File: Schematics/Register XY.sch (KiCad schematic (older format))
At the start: 0 parts

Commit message: Added XY register pair.
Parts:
- added C? (x4): 100nF, symbol Device:C
- added D? (x16): LED, symbol Device:LED
- added R? (x16): 220Ω, symbol Device:R
- added U? (x2): 74LS245, symbol 74xx:74LS245
- added U? (x2): 74F377, symbol 74xx:74LS377
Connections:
- new net: D?.1 (K), R?.1 (x16)
- new net AddressBus00: D?.2 (A), U?.19 (Q7), U?.9 (A7)
- new net AddressBus01: D?.2 (A), U?.16 (Q6), U?.8 (A6)
- new net AddressBus02: D?.2 (A), U?.15 (Q5), U?.7 (A5)
- new net AddressBus03: D?.2 (A), U?.12 (Q4), U?.6 (A4)
- new net AddressBus04: D?.2 (A), U?.5 (A3), U?.9 (Q3)
- new net AddressBus05: D?.2 (A), U?.4 (A2), U?.6 (Q2)
- new net AddressBus06: D?.2 (A), U?.3 (A1), U?.5 (Q1)
- new net AddressBus07: D?.2 (A), U?.2 (A0), U?.2 (Q0)
- new net AddressBus08: D?.2 (A), U?.19 (Q7), U?.9 (A7)
- new net AddressBus09: D?.2 (A), U?.16 (Q6), U?.8 (A6)
- new net AddressBus10: D?.2 (A), U?.15 (Q5), U?.7 (A5)
- new net AddressBus11: D?.2 (A), U?.12 (Q4), U?.6 (A4)
- new net AddressBus12: D?.2 (A), U?.5 (A3), U?.9 (Q3)
- new net AddressBus13: D?.2 (A), U?.4 (A2), U?.6 (Q2)
- new net AddressBus14: D?.2 (A), U?.3 (A1), U?.5 (Q1)
- new net AddressBus15: D?.2 (A), U?.2 (A0), U?.2 (Q0)
- new net DataBus00: U?.18 (B0), U?.18 (B0), U?.3 (D0), U?.3 (D0)
- new net DataBus01: U?.17 (B1), U?.17 (B1), U?.4 (D1), U?.4 (D1)
- new net DataBus02: U?.16 (B2), U?.16 (B2), U?.7 (D2), U?.7 (D2)
- new net DataBus03: U?.15 (B3), U?.15 (B3), U?.8 (D3), U?.8 (D3)
- new net DataBus04: U?.13 (D4), U?.13 (D4), U?.14 (B4), U?.14 (B4)
- new net DataBus05: U?.13 (B5), U?.13 (B5), U?.14 (D5), U?.14 (D5)
- new net DataBus06: U?.12 (B6), U?.12 (B6), U?.17 (D6), U?.17 (D6)
- new net DataBus07: U?.11 (B7), U?.11 (B7), U?.18 (D7), U?.18 (D7)
- new net GND: C?.2, C?.2, C?.2, C?.2, R?.2, R?.2, R?.2, R?.2, R?.2, R?.2, R?.2, R?.2, R?.2, R?.2, R?.2, R?.2, R?.2, R?.2, R?.2, R?.2, U?.10 (GND), U?.10 (GND), U?.10 (GND), U?.10 (GND)
- new net RegisterClock: U?.11 (CP), U?.11 (CP)
- new net VCC: C?.1, C?.1, C?.1, C?.1, U?.1 (A->B), U?.1 (A->B), U?.20 (VCC), U?.20 (VCC), U?.20 (VCC), U?.20 (VCC)
- new net ~XI: U?.1 (~E)
- new net ~XO: U?.19 (CE)
- new net ~YI: U?.1 (~E)
- new net ~YO: U?.19 (CE)

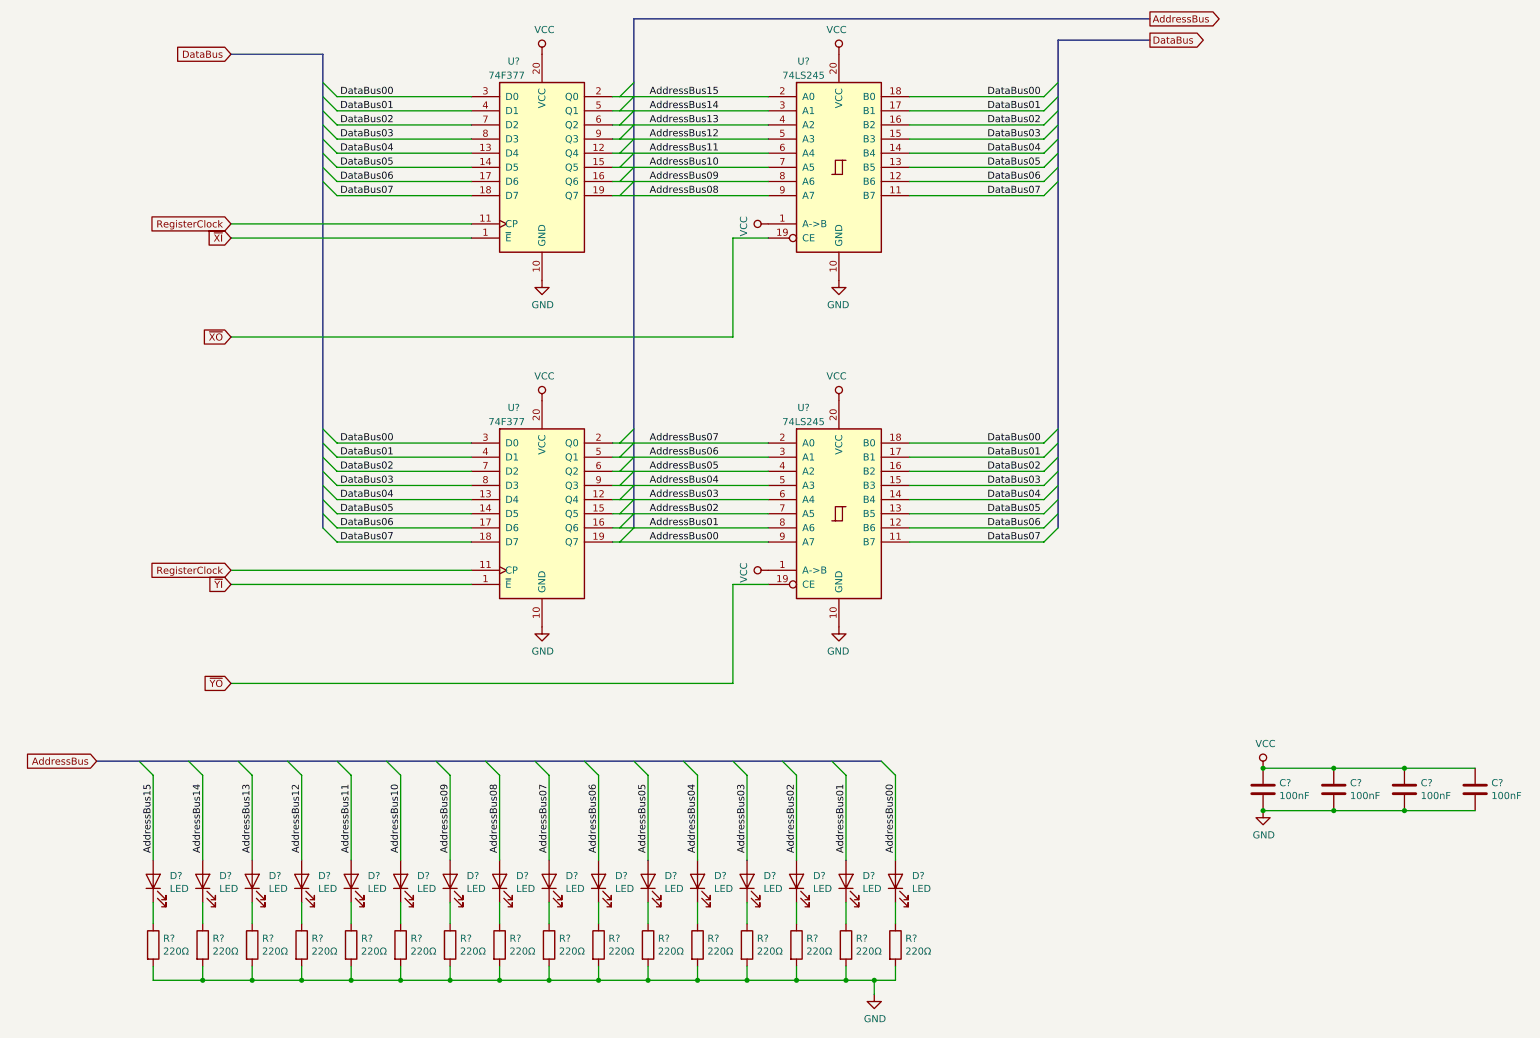
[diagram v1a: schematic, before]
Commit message: Ensure all pages are 8.5x11
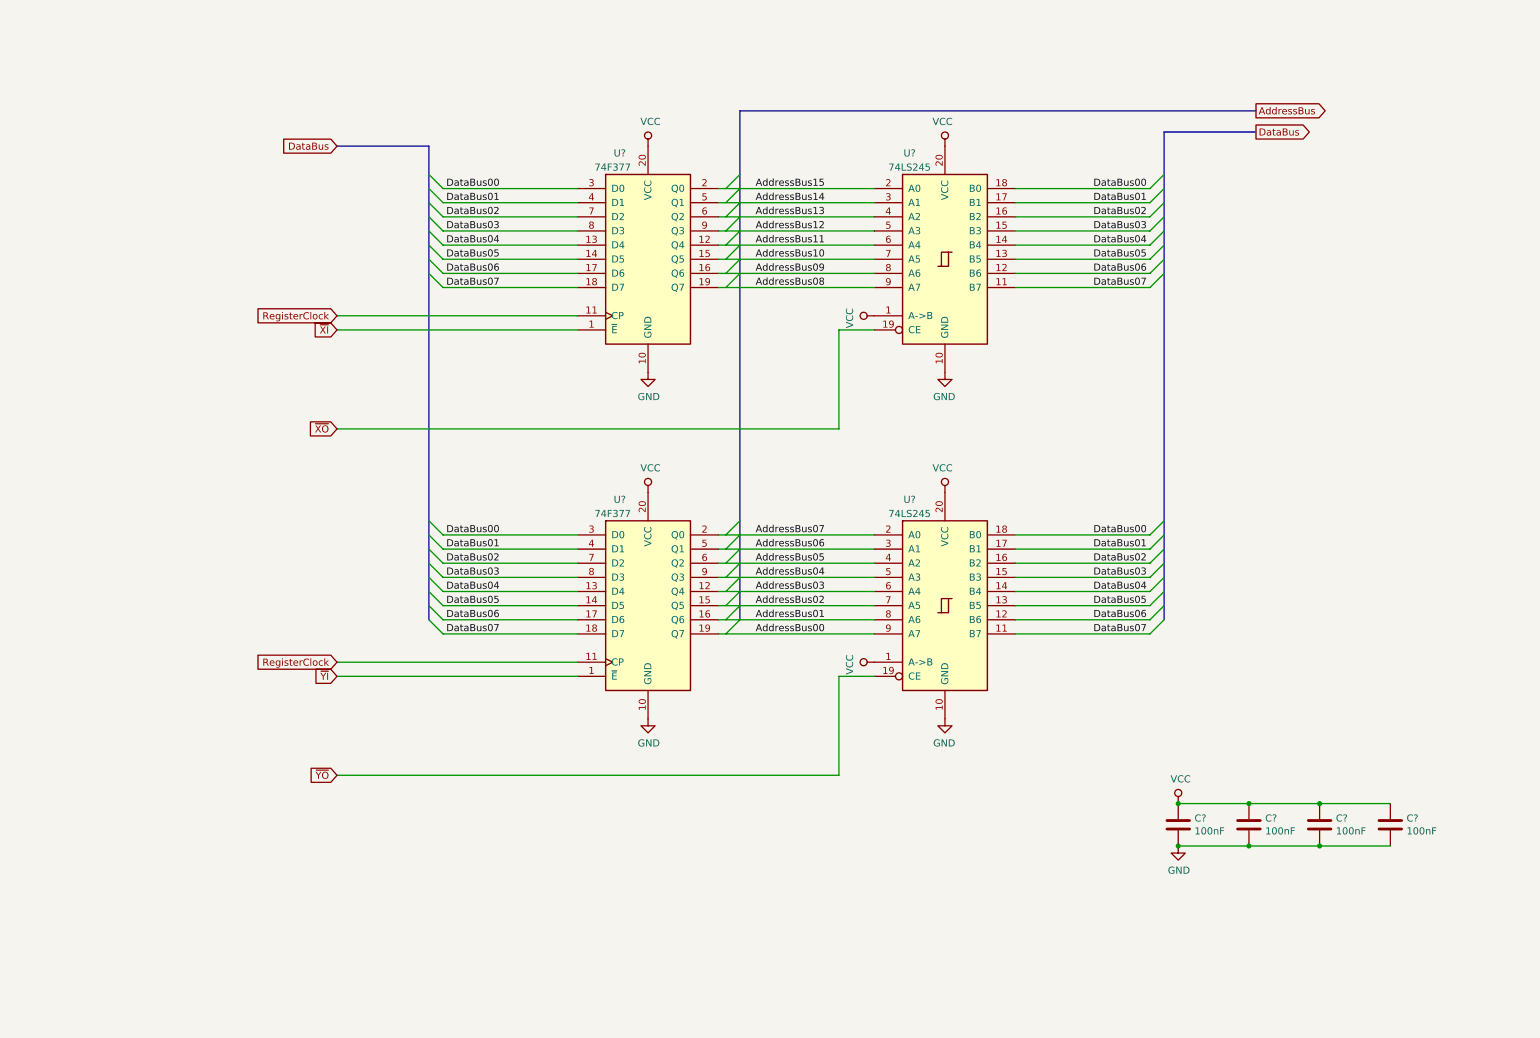
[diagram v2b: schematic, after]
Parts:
- removed D? (x16): LED, symbol Device:LED
- removed R? (x16): 220Ω, symbol Device:R
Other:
- moved on the sheet: C?, U?

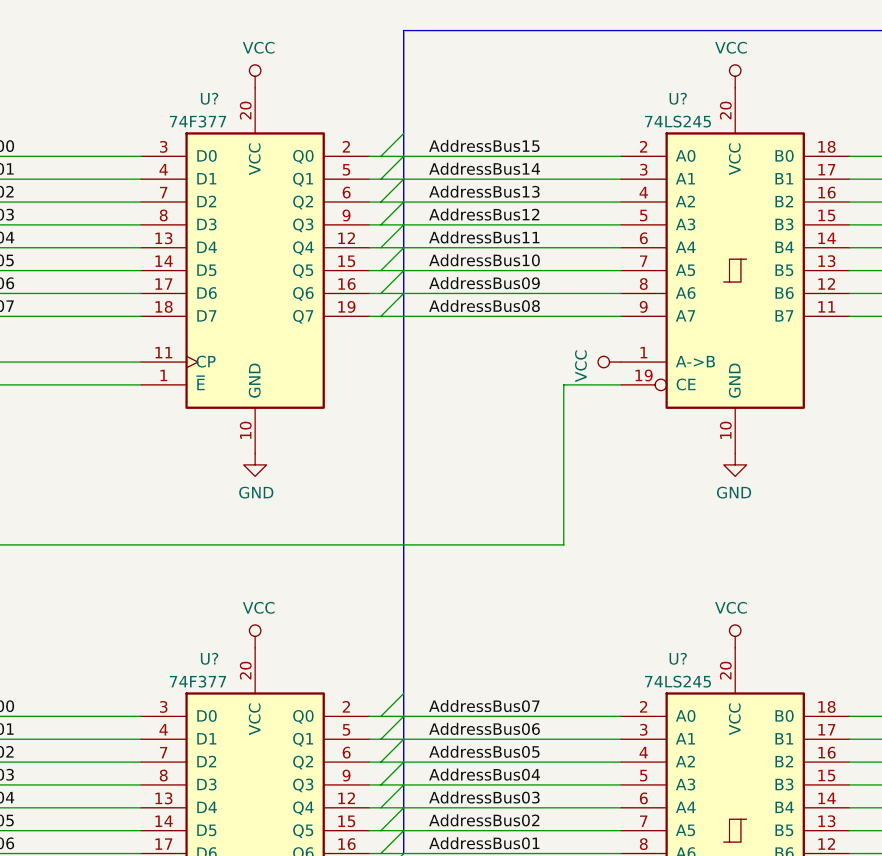
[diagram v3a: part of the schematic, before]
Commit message: Flesh out Register D, the device select register.
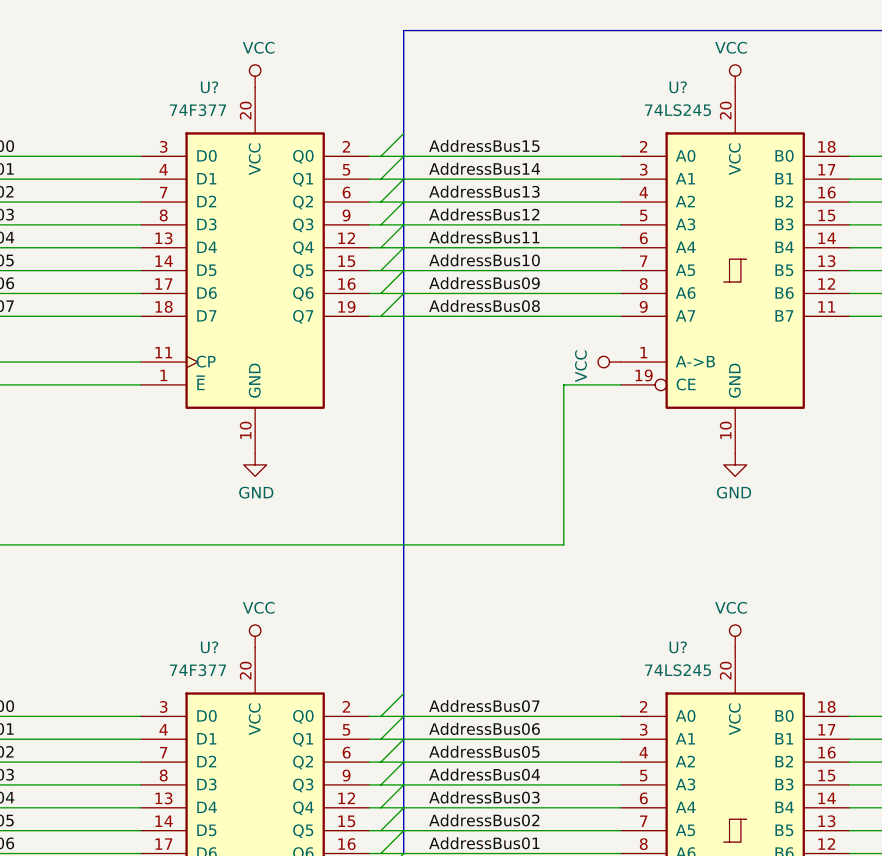
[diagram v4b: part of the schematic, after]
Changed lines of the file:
@@
 AR Path="/5D2C0CA7/5D836423" Ref="U?"  Part="1"
 AR Path="/5D7BD0EA/5D836423" Ref="U?"  Part="1"
-F 0 "U?" H 6750 3050 50  0000 C CNN
-F 1 "74LS245" H 6750 2950 50  0000 C CNN
+F 0 "U?" H 6750 3100 50  0000 C CNN
+F 1 "74LS245" H 6750 3000 50  0000 C CNN
 F 2 "" H 7000 2300 50  0001 C CNN
 F 3 "http://www.ti.com/lit/gpn/sn74LS245" H 7000 2300 50  0001 C CNN
@@
 AR Path="/5D2C0CA7/5D836429" Ref="U?"  Part="1"
 AR Path="/5D7BD0EA/5D836429" Ref="U?"  Part="1"
-F 0 "U?" H 4700 3050 50  0000 C CNN
-F 1 "74F377" H 4650 2950 50  0000 C CNN
+F 0 "U?" H 4700 3100 50  0000 C CNN
+F 1 "74F377" H 4650 3000 50  0000 C CNN
 F 2 "" H 4900 2300 50  0001 C CNN
 F 3 "http://www.ti.com/lit/gpn/sn74LS377" H 4900 2300 50  0001 C CNN
@@
 AR Path="/5D2C0CA7/5D908D96" Ref="U?"  Part="1"
 AR Path="/5D7BD0EA/5D908D96" Ref="U?"  Part="1"
-F 0 "U?" H 6750 5500 50  0000 C CNN
-F 1 "74LS245" H 6750 5400 50  0000 C CNN
+F 0 "U?" H 6750 5550 50  0000 C CNN
+F 1 "74LS245" H 6750 5450 50  0000 C CNN
 F 2 "" H 7000 4750 50  0001 C CNN
 F 3 "http://www.ti.com/lit/gpn/sn74LS245" H 7000 4750 50  0001 C CNN
@@
 AR Path="/5D2C0CA7/5D908DA2" Ref="U?"  Part="1"
 AR Path="/5D7BD0EA/5D908DA2" Ref="U?"  Part="1"
-F 0 "U?" H 4700 5500 50  0000 C CNN
-F 1 "74F377" H 4650 5400 50  0000 C CNN
+F 0 "U?" H 4700 5550 50  0000 C CNN
+F 1 "74F377" H 4650 5450 50  0000 C CNN
 F 2 "" H 4900 4750 50  0001 C CNN
 F 3 "http://www.ti.com/lit/gpn/sn74LS377" H 4900 4750 50  0001 C CNN

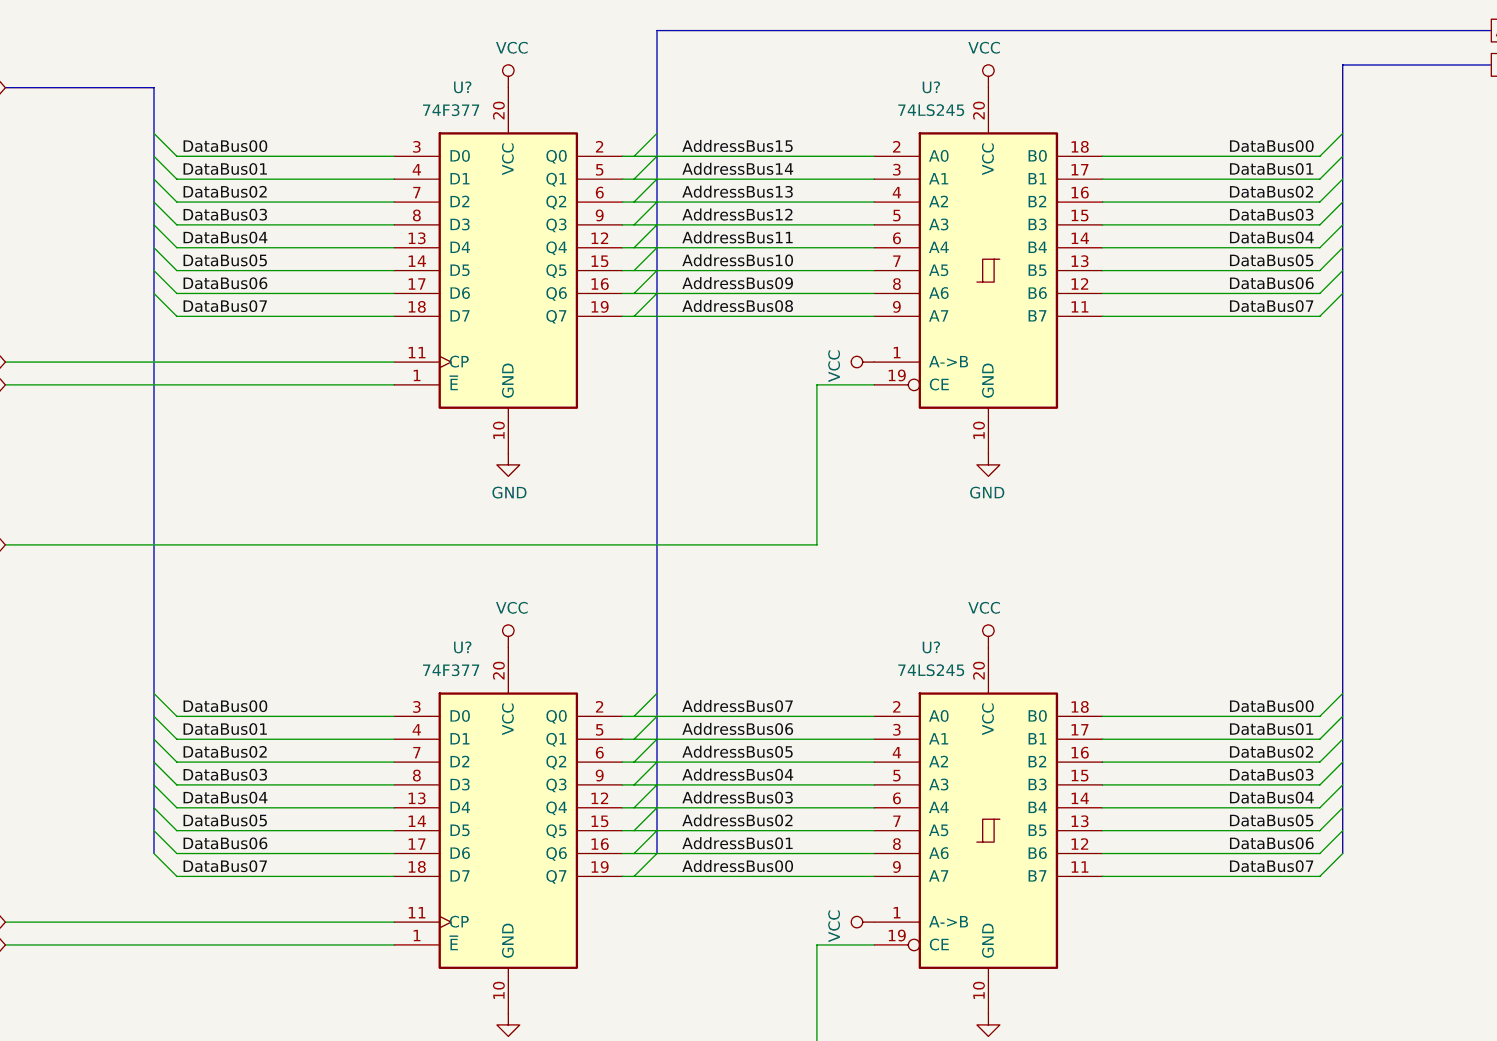
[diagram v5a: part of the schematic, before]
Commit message: Change net labels on buses to make them more consistent.
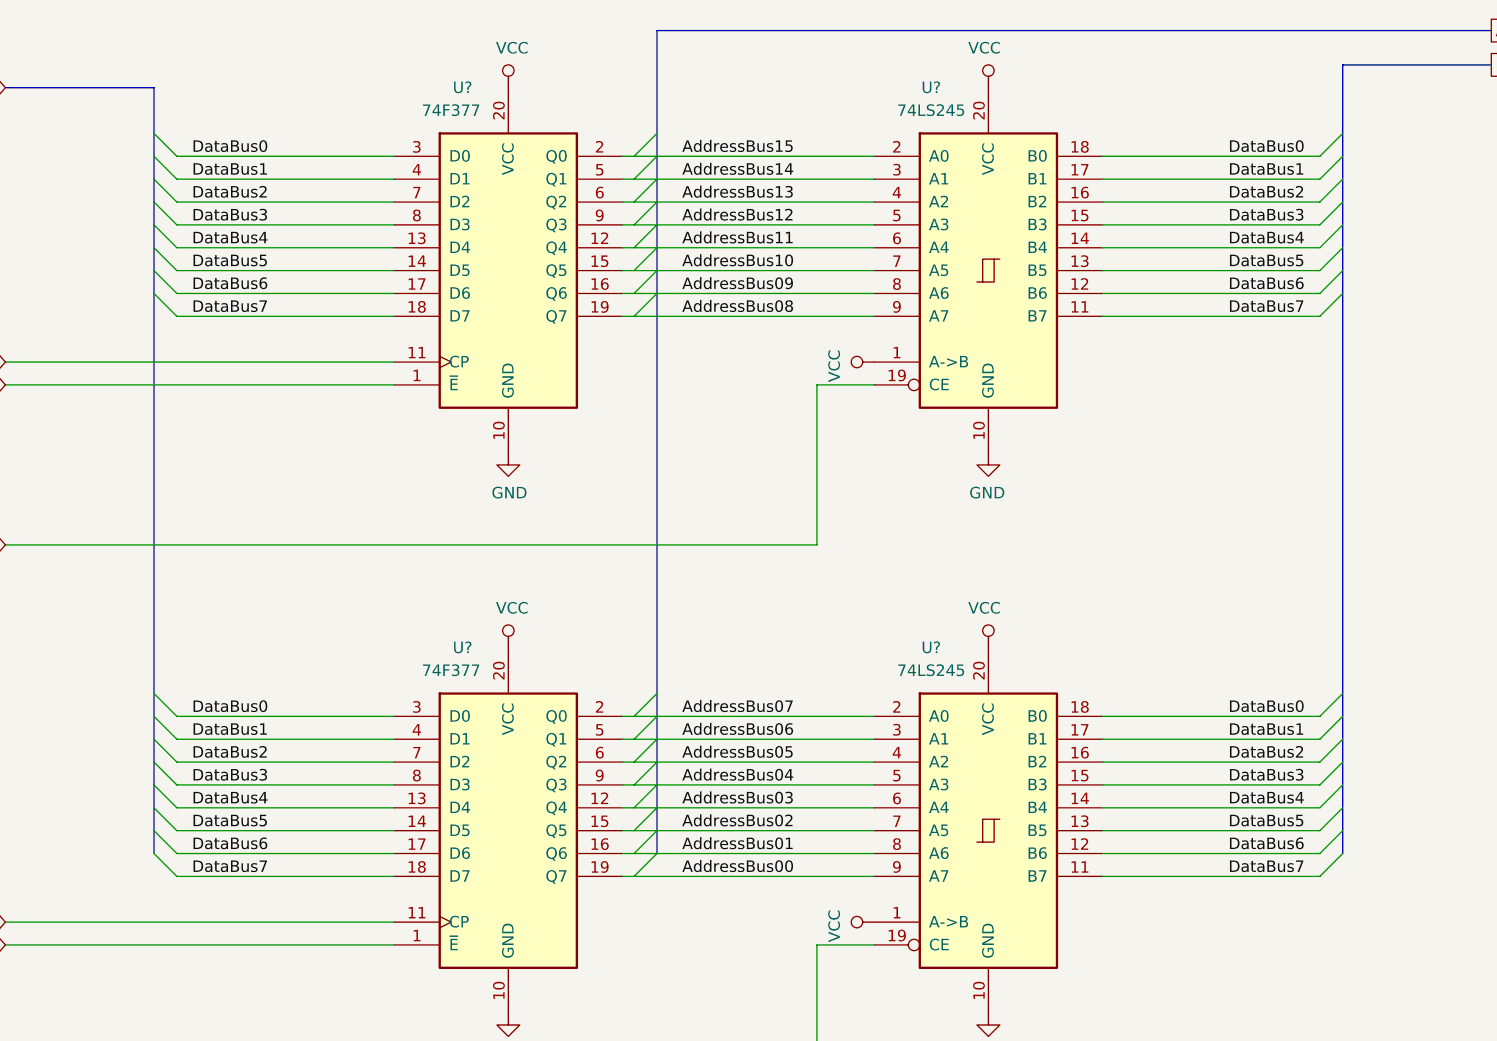
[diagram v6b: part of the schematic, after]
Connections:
- net DataBus00 renamed DataBus0
- net DataBus01 renamed DataBus1
- net DataBus02 renamed DataBus2
- net DataBus03 renamed DataBus3
- net DataBus04 renamed DataBus4
- net DataBus05 renamed DataBus5
- net DataBus06 renamed DataBus6
- net DataBus07 renamed DataBus7
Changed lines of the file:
@@
 	8550 1700 8450 1800
 Text Label 8050 1900 0    50   ~ 0
-DataBus01
+DataBus1
 Text Label 8050 2000 0    50   ~ 0
-DataBus02
+DataBus2
 Text Label 8050 2100 0    50   ~ 0
-DataBus03
+DataBus3
 Text Label 8050 2200 0    50   ~ 0
-DataBus04
+DataBus4
 Text Label 8050 2300 0    50   ~ 0
-DataBus05
+DataBus5
 Text Label 8050 2400 0    50   ~ 0
-DataBus06
+DataBus6
 Text Label 8050 2500 0    50   ~ 0
-DataBus07
+DataBus7
 Text Label 8050 1800 0    50   ~ 0
-DataBus00
+DataBus0
 $Comp
 L Device:C C?
@@
 	3350 1700 3450 1800
 Text Label 3850 1900 2    50   ~ 0
-DataBus01
+DataBus1
 Text Label 3850 2000 2    50   ~ 0
-DataBus02
+DataBus2
 Text Label 3850 2100 2    50   ~ 0
-DataBus03
+DataBus3
 Text Label 3850 2200 2    50   ~ 0
-DataBus04
+DataBus4
 Text Label 3850 2300 2    50   ~ 0
-DataBus05
+DataBus5
 Text Label 3850 2400 2    50   ~ 0
-DataBus06
+DataBus6
 Text Label 3850 2500 2    50   ~ 0
-DataBus07
+DataBus7
 Text Label 3850 1800 2    50   ~ 0
-DataBus00
+DataBus0
 Wire Wire Line
 	3450 2500 4400 2500
@@
 	8550 4150 8450 4250
 Text Label 8050 4350 0    50   ~ 0
-DataBus01
+DataBus1
 Text Label 8050 4450 0    50   ~ 0
-DataBus02
+DataBus2
 Text Label 8050 4550 0    50   ~ 0
-DataBus03
+DataBus3
 Text Label 8050 4650 0    50   ~ 0
-DataBus04
+DataBus4
 Text Label 8050 4750 0    50   ~ 0
-DataBus05
+DataBus5
 Text Label 8050 4850 0    50   ~ 0
-DataBus06
+DataBus6
 Text Label 8050 4950 0    50   ~ 0
-DataBus07
+DataBus7
 Text Label 8050 4250 0    50   ~ 0
-DataBus00
+DataBus0
 Wire Wire Line
 	8450 4950 7500 4950
@@
 	3350 4150 3450 4250
 Text Label 3850 4350 2    50   ~ 0
-DataBus01
+DataBus1
 Text Label 3850 4450 2    50   ~ 0
-DataBus02
+DataBus2
 Text Label 3850 4550 2    50   ~ 0
-DataBus03
+DataBus3
 Text Label 3850 4650 2    50   ~ 0
-DataBus04
+DataBus4
 Text Label 3850 4750 2    50   ~ 0
-DataBus05
+DataBus5
 Text Label 3850 4850 2    50   ~ 0
-DataBus06
+DataBus6
 Text Label 3850 4950 2    50   ~ 0
-DataBus07
+DataBus7
 Text Label 3850 4250 2    50   ~ 0
-DataBus00
+DataBus0
 Wire Wire Line
 	3450 4950 4400 4950
